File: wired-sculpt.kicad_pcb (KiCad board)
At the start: 2 copper layers, 40 x 50 mm, 39 parts, among them J1 10103594-0001LF, J2 FFC3B07-30-T, J3 AVR-ISP-6 - NOT FITTED, Q1 BSS84AK,215, Q2 2N7002BK, SW1 FSMSM, SW2 S2B-PH-K-S(LF)(SN), U1 USBLC6-2SC6, U2 LM2776DBVT, U3 AT90USB1286-AU, Y1 TSX-3225 16.0000MF18X-AC0

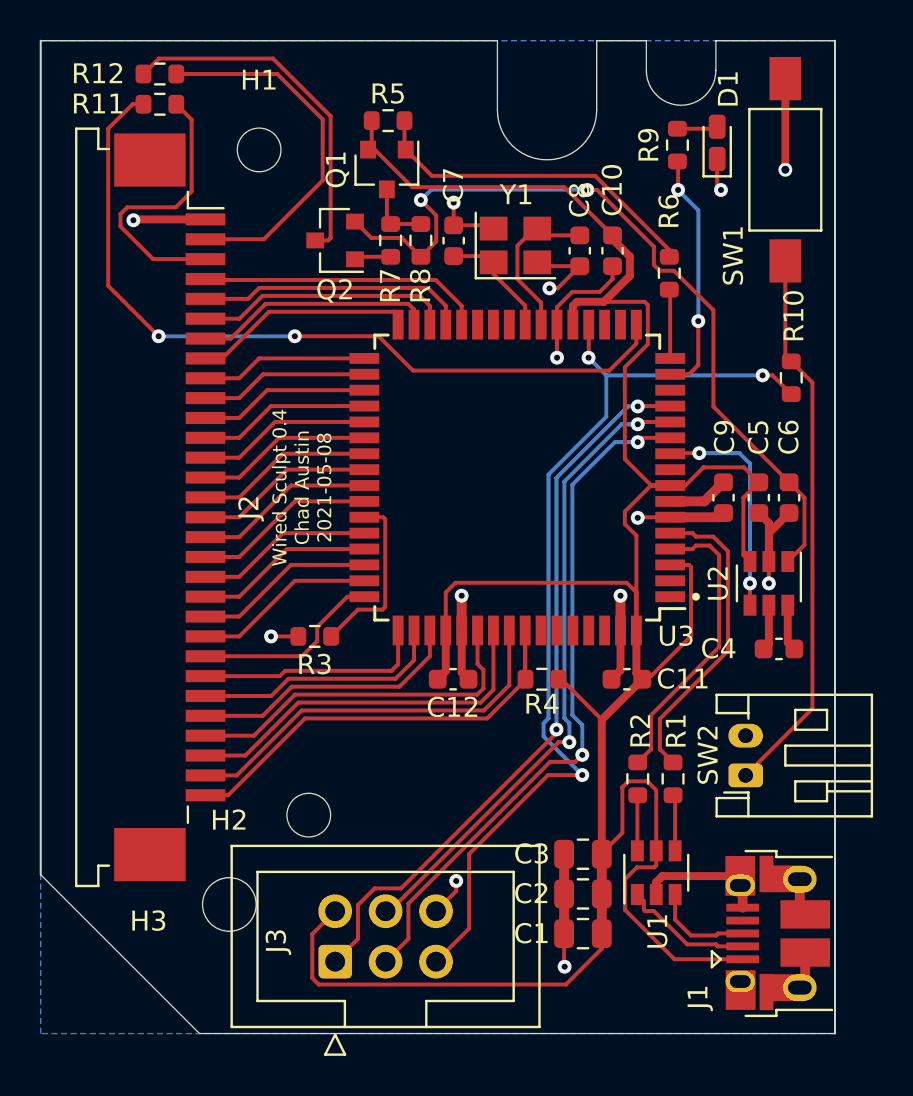
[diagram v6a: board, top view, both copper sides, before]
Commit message: The rev5 board design proposal.
Removed the charge pump.
When the common pin for both LEDs is driven with a 50% duty-cycle rectangular signal both LEDs can be used without additional circuit.
QMK has a feature to change the brightness of background LEDs and we are just going to use this feature to produce such a signal.

As the FN switch is also connected to this line we have to filter out the switching frequency to be able to read the switch.
For this a simple diode rectifier was added. A resistor to discharge the filter capacitor is also needed to detect the switch off state.
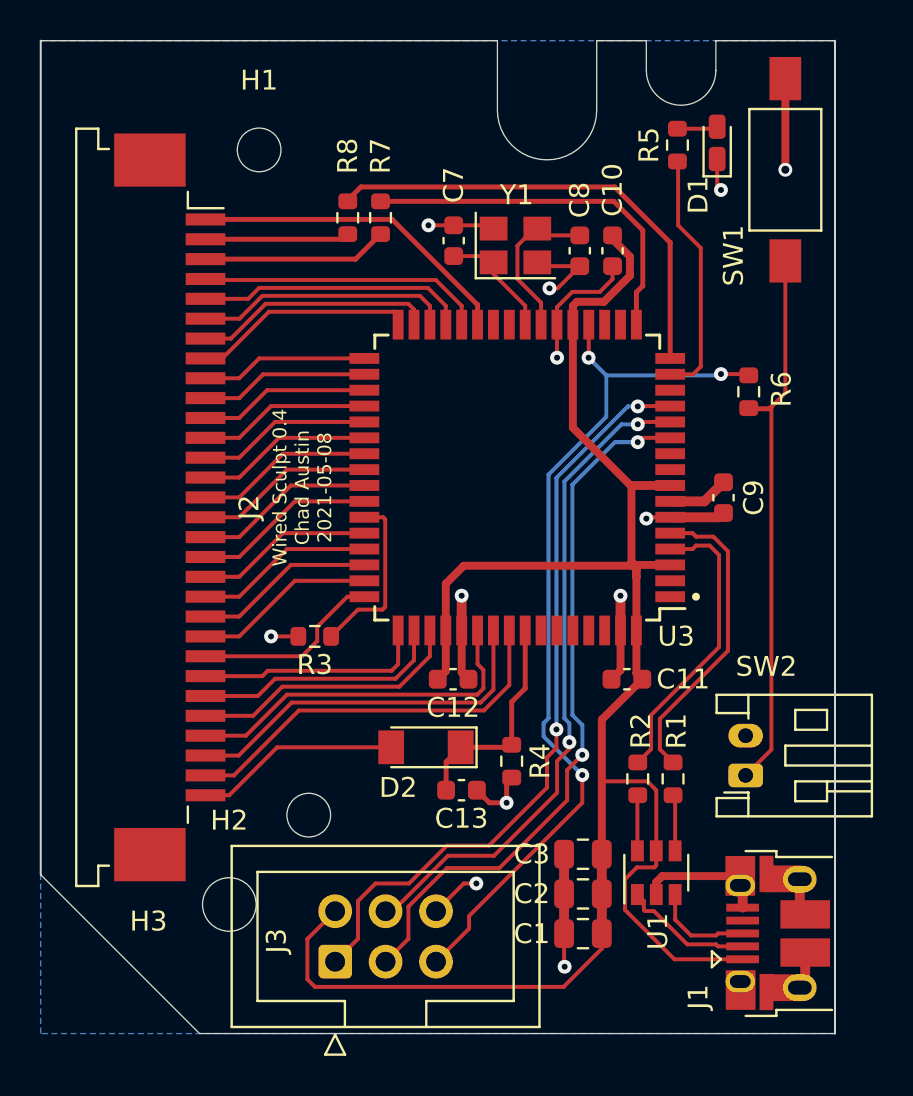
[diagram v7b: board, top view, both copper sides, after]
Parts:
- removed C4, C5, C6: CL10A105KA8NNNC, Capacitor_SMD:C_0603_1608Metric
- removed Q1: BSS84AK,215, Package_TO_SOT_SMD:SOT-23
- removed Q2: 2N7002BK, Package_TO_SOT_SMD:SOT-23
- removed the R5 at (137.5, 34.0)
- removed the R6 at (151.7, 41.7)
- removed the R7 at (137.6, 40.1)
- removed the R8 at (139.1, 40.1)
- removed U2: LM2776DBVT, Package_TO_SOT_SMD:SOT-23-6
- added C13: CL10B104KB8NNNC, Capacitor_SMD:C_0603_1608Metric, F.Cu at (141.2, 67.7)
- added D2: LL4148, Diode_SMD:D_MiniMELF, F.Cu at (139.4, 65.6)
- C7, C8: value 06035A160JAT2A -> CL10C160JB8NNNC
- R4: value ERJ-3EKF8873V -> ERJ-PA3J155V
- R7: renamed from R11; value ERJ-PA3J560V -> ERJ-PA3J151V
- R8: renamed from R12; value ERJ-PA3F22R0V -> ERJ-PA3J151V
- moved R7 12.5 mm to (137.1, 38.9), turned to -90 degrees
- moved R8 11.9 mm to (135.5, 38.9), turned to -90 degrees
- moved R4 4.40 mm to (143.7, 66.3), turned to -90 degrees
- moved R6 2.26 mm to (155.7, 47.7), turned to -90 degrees
- renumbered R9 to R5, R10 to R6
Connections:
- J1 pad 4: Net-(J1-Pad4) -> unconnected-(J1-Pad4)
- J2 pad 1: GND -> Net-(J2-Pad1)
- J2 pad 30: PF4 -> Net-(J2-Pad30)
- R4 pad 1: VBUS -> PF4
- R4 pad 2: PF4 -> GND
- U3 pad 1: Net-(U3-Pad1) -> unconnected-(U3-Pad1)
- U3 pad 10: PB0 -> unconnected-(U3-Pad10)
- U3 pad 14: Net-(U3-Pad14) -> unconnected-(U3-Pad14)
- U3 pad 16: GREEN+ -> GREEN-
- U3 pad 18: Net-(U3-Pad18) -> unconnected-(U3-Pad18)
- U3 pad 19: Net-(U3-Pad19) -> unconnected-(U3-Pad19)
- U3 pad 2: Net-(U3-Pad2) -> unconnected-(U3-Pad2)
- U3 pad 25: Net-(U3-Pad25) -> unconnected-(U3-Pad25)
- U3 pad 26: Net-(U3-Pad26) -> unconnected-(U3-Pad26)
- U3 pad 27: Net-(U3-Pad27) -> Net-(J2-Pad1)
- U3 pad 58: Net-(U3-Pad58) -> unconnected-(U3-Pad58)
- U3 pad 59: Net-(U3-Pad59) -> unconnected-(U3-Pad59)
- U3 pad 60: Net-(U3-Pad60) -> unconnected-(U3-Pad60)
- U3 pad 61: Net-(U3-Pad61) -> unconnected-(U3-Pad61)
- U3 pad 62: Net-(U3-Pad62) -> unconnected-(U3-Pad62)
- U3 pad 9: Net-(U3-Pad9) -> unconnected-(U3-Pad9)
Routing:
- net -5V: track 40.5 -> 0.00 mm, vias 2 -> 0
- net VBUS: track 138.6 -> 102.2 mm
- net RED+: track 40.1 -> 18.7 mm, vias 2 -> 0
- net Net-(Q1-Pad1): track 17.2 -> 0.00 mm
- net Net-(J2-Pad1): track 0.00 -> 16.5 mm
- net PF4: track 24.0 -> 10.7 mm
- net PB0: track 11.4 -> 0.00 mm, vias 2 -> 0
- net Net-(J2-Pad2): track 18.5 -> 7.27 mm
- net Net-(J2-Pad30): track 0.00 -> 9.51 mm
- net GND: track 62.8 -> 56.0 mm, vias 13 -> 12
- net Net-(J2-Pad3): track 15.2 -> 9.34 mm
- net GREEN-: track 17.9 -> 23.6 mm
- net Net-(Q1-Pad3): track 3.60 -> 0.00 mm
- net RST: track 48.3 -> 44.8 mm
- net GREEN+: track 3.48 -> 0.00 mm
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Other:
- net class Default removed
- net class Fat removed
